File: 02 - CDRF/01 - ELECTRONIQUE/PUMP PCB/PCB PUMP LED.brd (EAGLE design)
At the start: 25 x 25 mm, 13 parts, among them J3 PWRPAD2-5MM, J4 PWRPAD2-5MM

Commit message: update
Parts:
- moved R4 11.5 mm to (16.3, 5.08), flipped to the bottom, turned to 270 degrees
- moved R2 9.71 mm to (8.31, 5.17), flipped to the bottom
- moved T1 3.06 mm to (7.11, 4.83)
- moved R1 2.97 mm to (10.7, 4.32)
- moved PAD3 1.98 mm to (20.3, 10.8)
- moved D2 1.14 mm to (3.37, 17.7), turned to 60 degrees
- moved R3 0.57 mm to (13.7, 4.32)
- moved D1 0.57 mm to (22.4, 8.89), turned to 70 degrees
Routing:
- net EV: track 5.62 -> 16.2 mm
- net GND: track 0.00 -> 9.73 mm
- net PUMP: track 6.34 -> 15.7 mm
- net N$3: track 14.5 -> 7.32 mm, vias 2 -> 1
- net N$2: track 7.98 -> 12.7 mm
- net N$4: track 14.4 -> 10.6 mm, vias 0 -> 1
- net +5V: track 33.5 -> 32.7 mm
- removed copper zone on layer 1, net GND

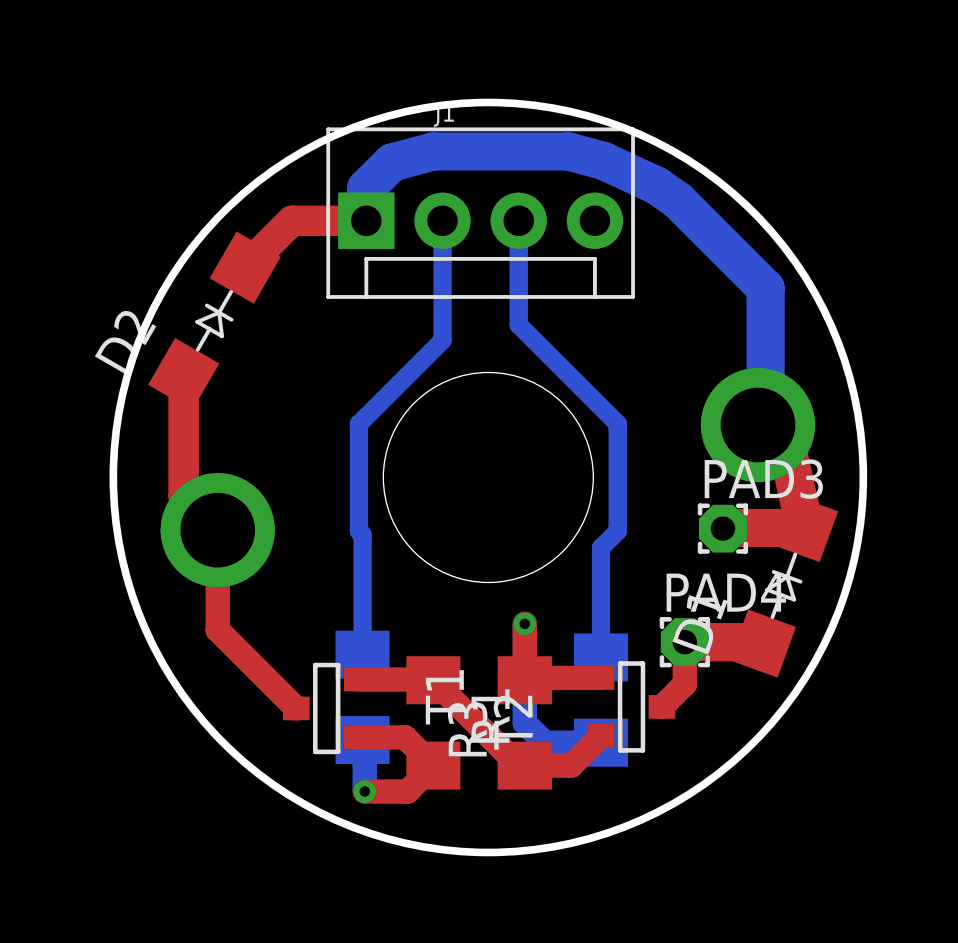
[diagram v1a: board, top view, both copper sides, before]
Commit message: update 3D packages
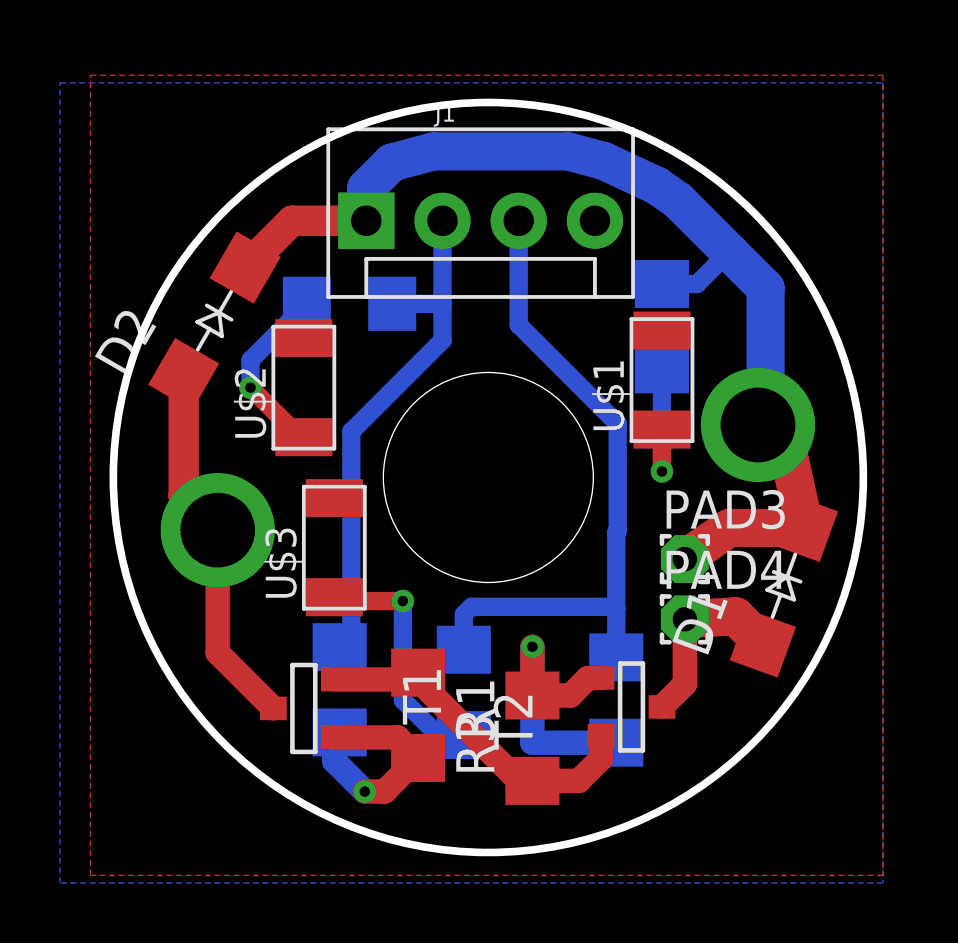
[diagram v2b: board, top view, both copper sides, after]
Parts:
- added R5, R6, R7: 1K, rcl:R1206
- added U$1, U$2, U$3: LEDFAB1206, fab:LED1206FAB
- J1: device CONNECTORS:MOLEX-1X4 -> OPENBOT:MOLEX-1X4
- moved PAD3 1.63 mm to (19.1, 9.78)
- moved R2 0.80 mm to (7.55, 5.42)
- moved PAD4 0.76 mm to (19.1, 7.77)
- moved T1 0.76 mm to (6.35, 4.83)
- moved R3 0.57 mm to (14.0, 3.81)
- moved R1 0.57 mm to (10.2, 4.57)
- moved R4 0.51 mm to (16.8, 5.08)
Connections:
- new net N$5: R5.1, U$1.1
- new net N$6: R6.1, U$2.1
- new net N$7: R7.1, U$3.1
- net +5V: now also R5.2
- net EV: now also R7.2
- net GND: now also U$1.2, U$2.2, U$3.2
- net PUMP: now also R6.2
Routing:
- net N$7: track 0.00 -> 8.16 mm, vias 0 -> 1
- net EV: track 16.2 -> 22.3 mm
- net N$6: track 0.00 -> 6.03 mm, vias 0 -> 1
- net N$5: track 0.00 -> 4.80 mm, vias 0 -> 1
- net +5V: track 32.7 -> 37.0 mm
- net GND: track 9.73 -> 11.7 mm
- net PUMP: track 15.7 -> 17.3 mm
- net N$1: track 5.12 -> 6.22 mm
- added copper zone on layer 1, net GND
- added copper zone on layer 16, net GND
